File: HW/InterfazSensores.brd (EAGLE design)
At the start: 160 x 100 mm, 30 parts, among them IC1 LM2940, T1 BC846, T2 BC846, T3 BC846

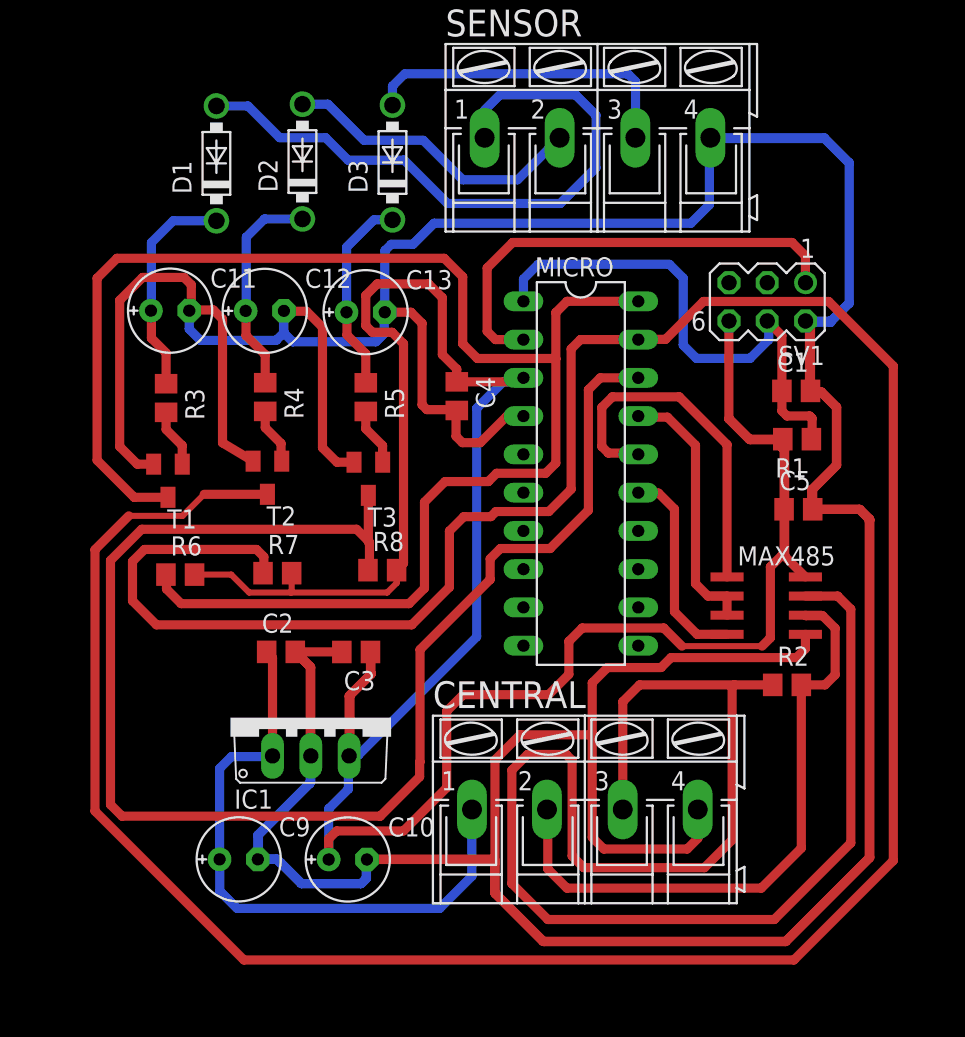
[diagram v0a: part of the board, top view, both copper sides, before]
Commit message: Acomodo HW
Renombra archivos y elimina duplicados
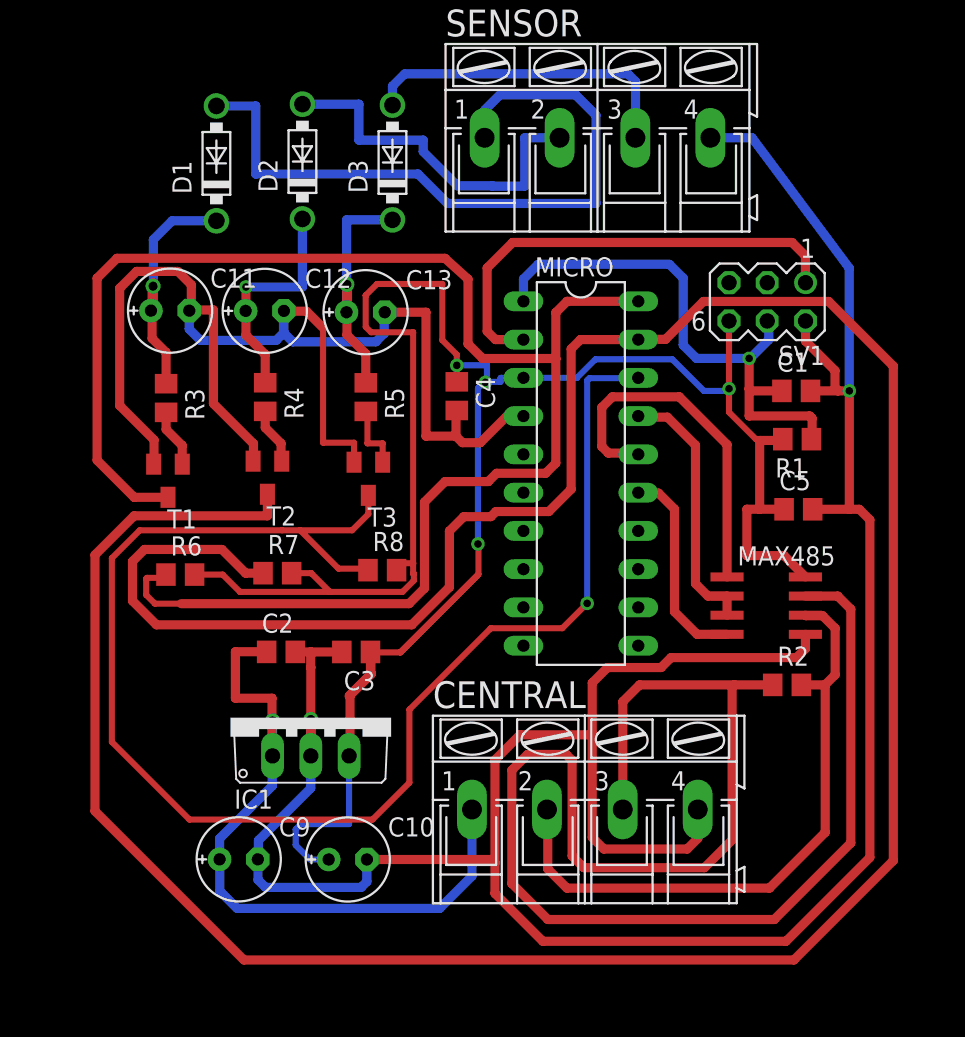
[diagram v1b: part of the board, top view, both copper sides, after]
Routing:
- net GND: track 414.0 -> 273.4 mm, vias 3 -> 1
- net VCC: track 185.7 -> 154.7 mm, vias 1 -> 3
- net N$1: track 41.6 -> 49.4 mm
- net N$9: track 13.3 -> 18.3 mm
- net N$5: track 20.3 -> 24.4 mm
- net N$4: track 42.5 -> 46.6 mm
- net N$7: track 14.7 -> 18.6 mm
- net SENSOR1: track 104.4 -> 107.0 mm
- net RST: track 35.1 -> 36.9 mm, vias 0 -> 1
- net N$2: track 41.2 -> 42.2 mm
- net N$8: track 14.4 -> 15.2 mm, vias 0 -> 1
- net SENSOR3: track 97.5 -> 98.2 mm, vias 0 -> 1
- net N$10: track 3.83 -> 4.49 mm

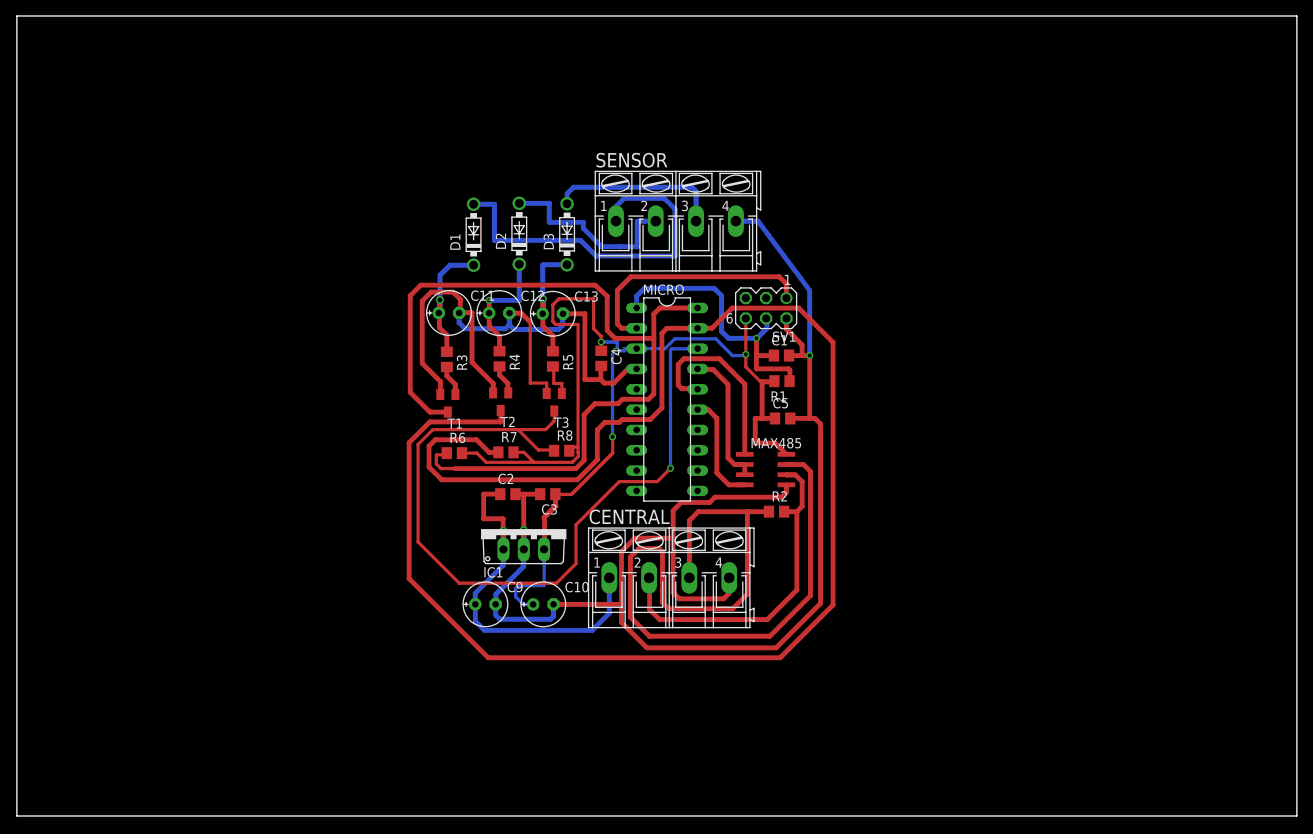
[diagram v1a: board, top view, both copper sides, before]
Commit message: Correcciones
Corregimos en placa algunas inconsistencias
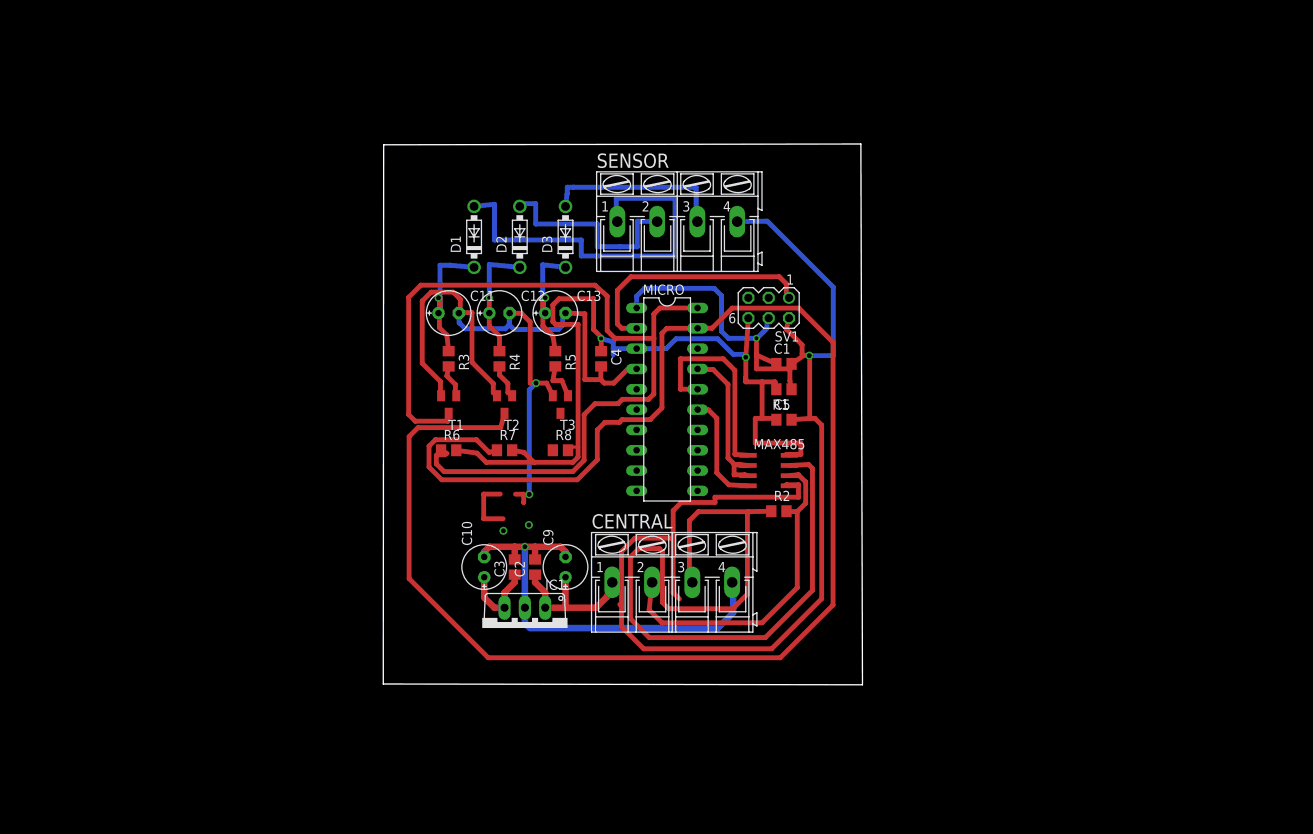
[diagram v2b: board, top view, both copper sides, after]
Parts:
- CENTRAL: value (none) -> central
- MICRO: value (none) -> SH8
- SENSOR: value (none) -> sensor
- SV1: value (none) -> BDM
- moved IC1 12.4 mm to (63.5, 23.5), turned to 180 degrees
- moved C9 11.0 mm to (68.6, 31.1), turned to 90 degrees
- moved C3 10.0 mm to (62.2, 31.1), turned to 90 degrees
- moved C2 9.73 mm to (64.8, 31.1), turned to 90 degrees
- moved C10 8.74 mm to (58.4, 31.1), turned to 90 degrees
- moved C1 1.09 mm to (95.9, 56.5)
- moved R1 1.04 mm to (95.9, 53.3)
- moved T3 0.82 mm to (67.9, 51.4)
- moved R6 0.80 mm to (54.0, 45.7)
- moved CENTRAL 0.67 mm to (81.9, 29.2)
- moved T2 0.60 mm to (61.0, 51.4)
- moved MAX485 0.41 mm to (94.0, 43.2)
- moved D2 0.39 mm to (62.9, 72.4)
- moved D3 0.38 mm to (68.6, 72.4)
- moved C13 0.33 mm to (67.3, 62.9)
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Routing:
- net SENSOR3: track 98.2 -> 0.26 mm, vias 1 -> 0
- net GND: track 273.4 -> 306.4 mm, vias 1 -> 4
- net VCC: track 154.7 -> 122.2 mm, vias 3 -> 2
- net N$1: track 49.4 -> 26.3 mm
- net SENSOR1: track 107.0 -> 112.0 mm
- net CONTROL485: track 17.5 -> 21.4 mm
- net N$4: track 46.6 -> 49.2 mm
- net RST: track 36.9 -> 38.5 mm
- net N$5: track 24.4 -> 26.0 mm
- net RXD: track 23.9 -> 25.5 mm
- net N$6: track 21.7 -> 23.0 mm
- net N$3: track 102.6 -> 103.7 mm
- net N$7: track 18.6 -> 19.5 mm
- net SENSOR2: track 205.4 -> 206.1 mm
- net N$12: track 3.76 -> 4.36 mm
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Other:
- board size 160 x 100 mm -> 59.9 x 67.6 mm

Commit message: Redistribucion
Cambio layout del PCB, para rutear
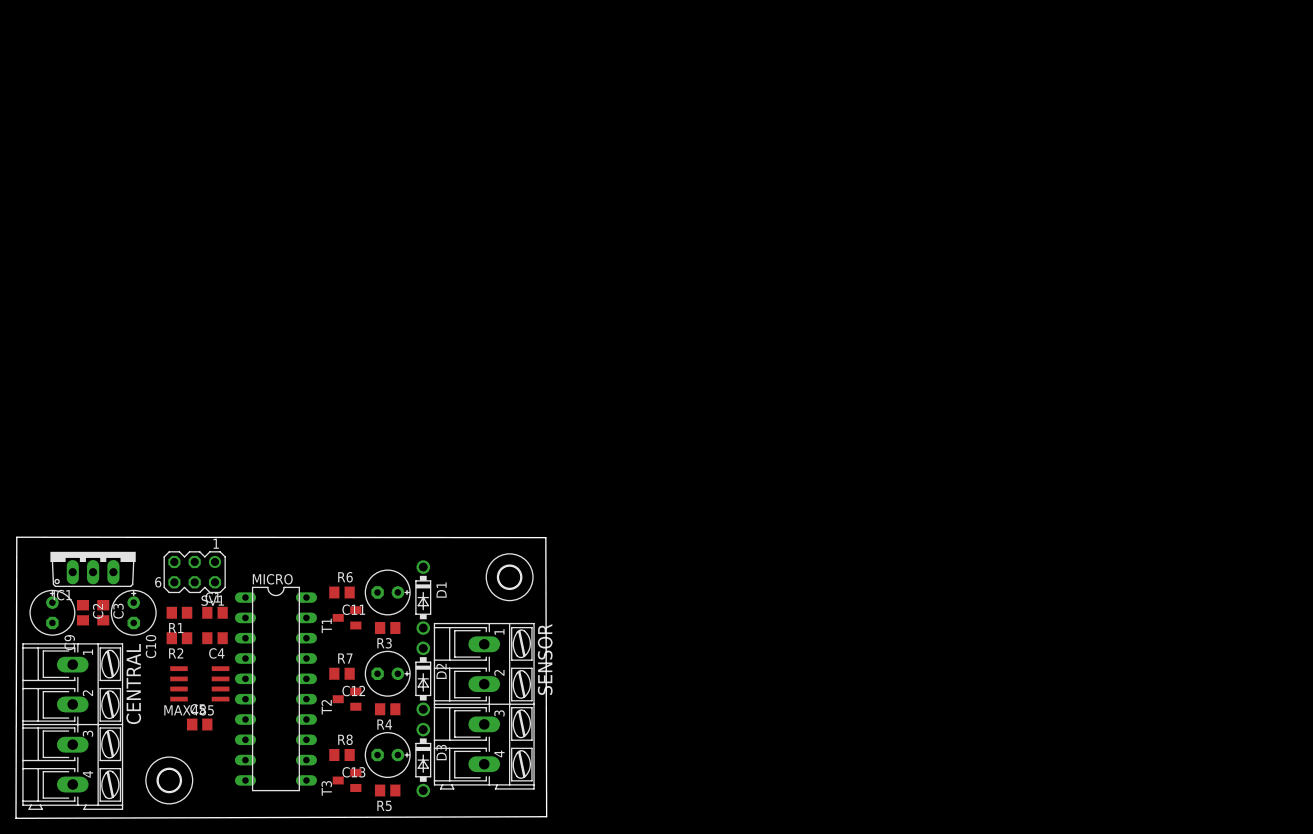
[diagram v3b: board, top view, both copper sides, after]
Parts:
- added U$1, U$3: (no value), holes:2,8
- moved C5 82.4 mm to (22.9, 11.4)
- moved R1 80.6 mm to (20.3, 25.4)
- moved SV1 79.0 mm to (22.2, 30.5)
- moved C1 77.6 mm to (24.8, 25.4)
- moved CENTRAL 77.0 mm to (6.99, 11.4), turned to 270 degrees
- moved R2 76.6 mm to (20.3, 22.2), turned to 180 degrees
- moved MAX485 76.0 mm to (22.9, 16.5), turned to 90 degrees
- moved D3 67.8 mm to (50.8, 6.99), turned to 270 degrees
- moved SENSOR 65.0 mm to (58.4, 14.0), turned to 270 degrees
- moved C9 64.4 mm to (4.45, 25.4), turned to 270 degrees
- moved MICRO 60.8 mm to (32.4, 15.9)
- moved C4 59.6 mm to (24.8, 22.2), turned to 180 degrees
- moved C13 59.1 mm to (46.4, 7.62), turned to 180 degrees
- moved R5 57.9 mm to (46.4, 3.17), turned to 180 degrees
- moved C2 56.8 mm to (8.26, 25.4), turned to 270 degrees
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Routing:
- net GND: track 306.4 -> 0.00 mm, vias 4 -> 0
- net SENSOR2: track 206.1 -> 0.00 mm
- net VCC: track 122.2 -> 0.00 mm, vias 2 -> 0
- net SENSOR1: track 112.0 -> 0.00 mm
- net N$3: track 103.7 -> 0.00 mm
- net N$4: track 49.2 -> 0.00 mm
- net N$2: track 42.4 -> 0.00 mm
- net RST: track 38.5 -> 0.00 mm, vias 1 -> 0
- net BKGD: track 31.1 -> 0.00 mm
- net N$1: track 26.3 -> 0.00 mm
- net N$5: track 26.0 -> 0.00 mm
- net RXD: track 25.5 -> 0.00 mm
- net N$6: track 23.0 -> 0.00 mm
- net CONTROL485: track 21.4 -> 0.00 mm
- net N$7: track 19.5 -> 0.00 mm
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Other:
- board size 59.9 x 67.6 mm -> 66.3 x 35.1 mm

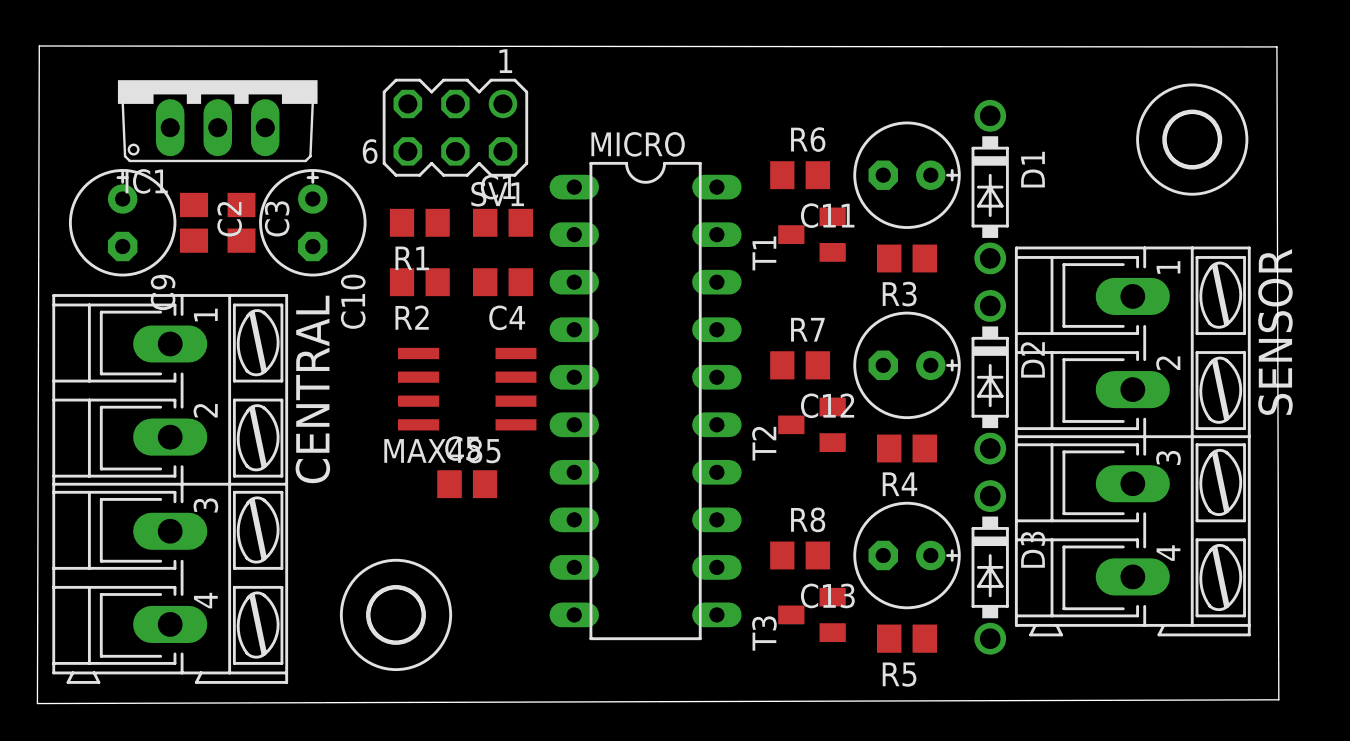
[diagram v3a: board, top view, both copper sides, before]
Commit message: Cambios efectuados en el board
Cambios que hice en el brd por un problema de grilla.
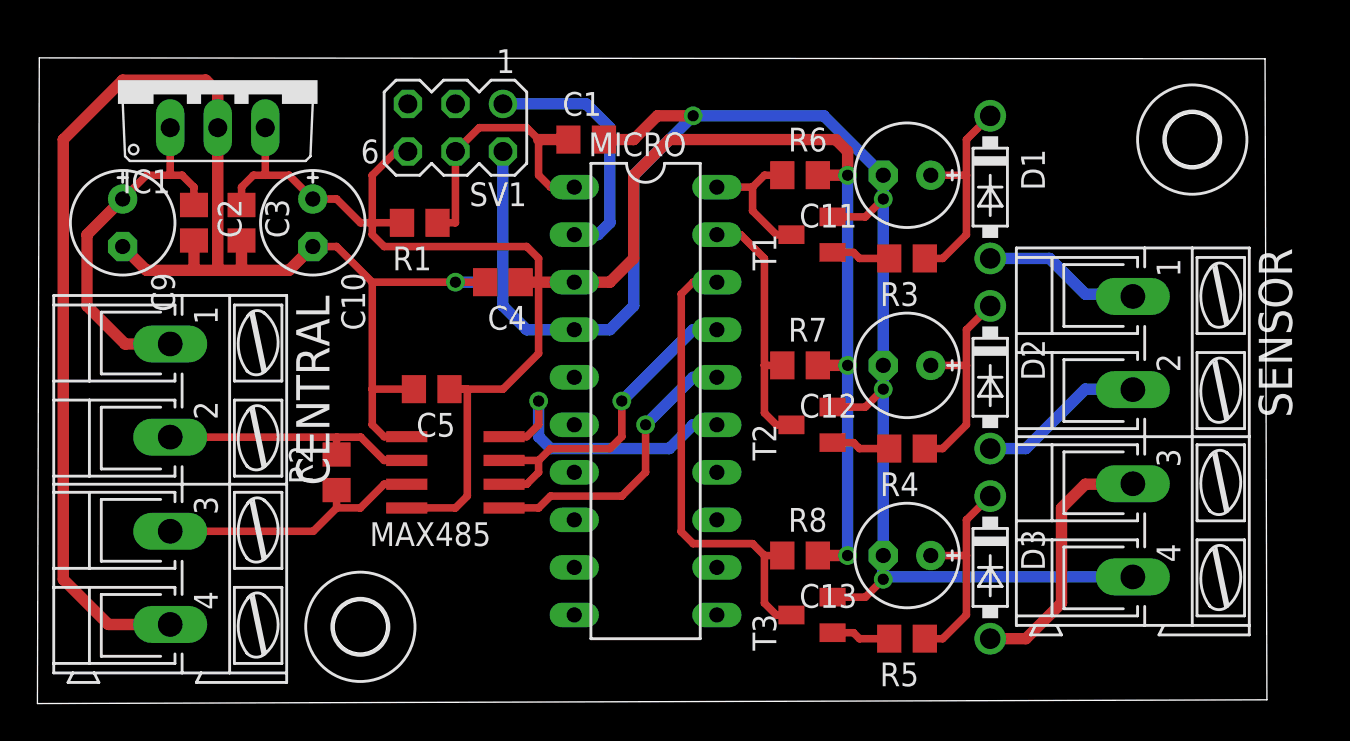
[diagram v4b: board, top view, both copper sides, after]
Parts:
- moved R2 11.1 mm to (15.9, 12.1), turned to 90 degrees
- moved C1 6.29 mm to (29.2, 29.8)
- moved C5 5.43 mm to (21.0, 16.5), turned to 180 degrees
- moved MAX485 4.49 mm to (22.2, 12.1)
- moved U$3 2.01 mm to (17.1, 3.81)
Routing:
- net GND: track 0.00 -> 182.4 mm, vias 0 -> 5
- net VCC: track 0.00 -> 99.1 mm, vias 0 -> 3
- net SENSOR3: track 0.00 -> 25.0 mm
- net N$1: track 0.00 -> 19.9 mm
- net CONTROL485: track 0.00 -> 18.1 mm, vias 0 -> 1
- net RXD: track 0.00 -> 15.8 mm, vias 0 -> 1
- net RST: track 0.00 -> 15.7 mm
- net TXD: track 0.00 -> 15.6 mm, vias 0 -> 1
- net N$3: track 0.00 -> 14.6 mm
- net N$2: track 0.00 -> 14.1 mm
- net N$6: track 0.00 -> 14.0 mm
- net SENSOR2: track 0.00 -> 14.0 mm
- net BKGD: track 0.00 -> 13.5 mm
- net N$9: track 0.00 -> 11.5 mm
- net N$8: track 0.00 -> 11.5 mm
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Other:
- board size 66.3 x 35.1 mm -> 65.7 x 34.5 mm

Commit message: Cambios realizados en el board
Placa board actualizada
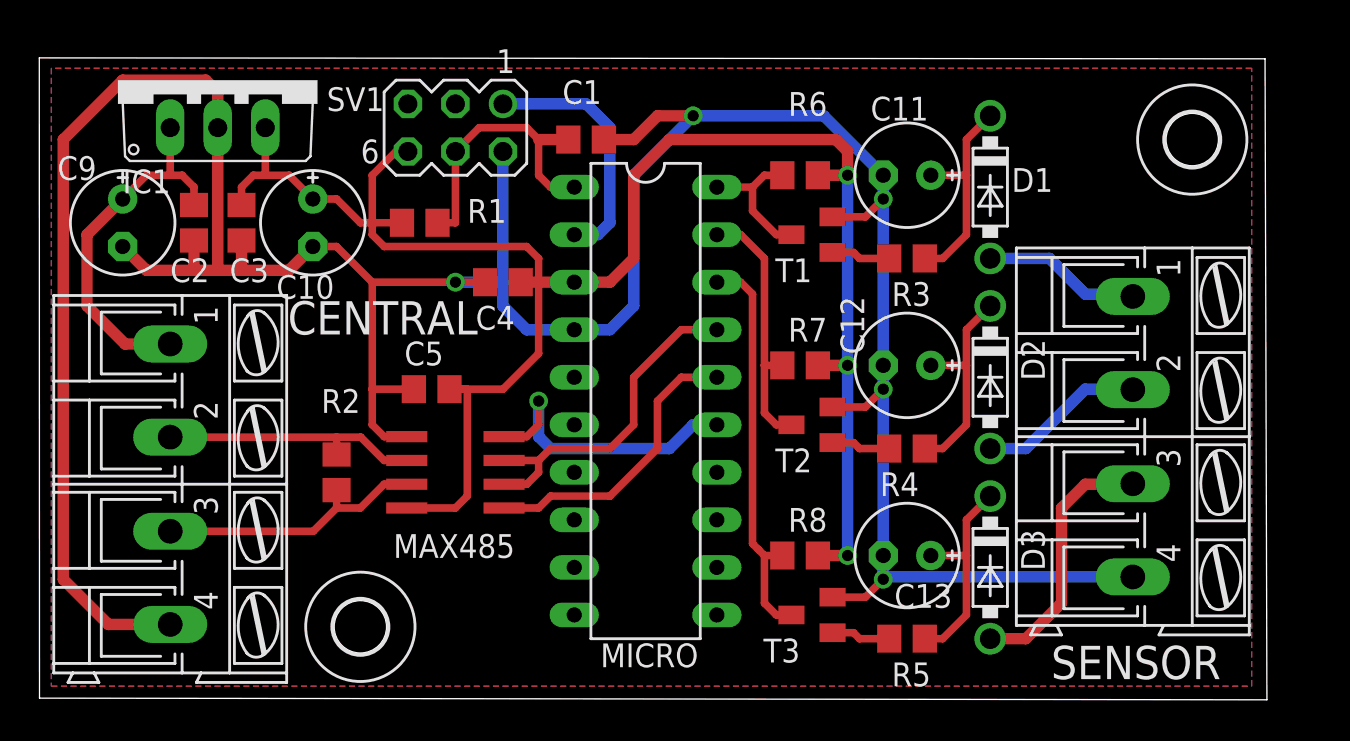
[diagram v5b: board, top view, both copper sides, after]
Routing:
- net SENSOR3: track 25.0 -> 21.6 mm
- net CONTROL485: track 18.1 -> 18.5 mm, vias 1 -> 0
- net RXD: vias 1 -> 0
- added copper zone on layer 1, net GND
- added copper zone on layer 16, net N$11
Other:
- board size 65.7 x 34.5 mm -> 65.6 x 34.3 mm
